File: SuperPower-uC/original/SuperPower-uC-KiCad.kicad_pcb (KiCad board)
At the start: 2 copper layers, 95 x 42 mm, 172 parts, among them J1 JST_PH_S2B_thru, J11 Conn_01x02_Male, J12 Conn_01x02_Male, J13 Conn_01x02_Male, J2 Barrel_Jack_Switch, J3 Conn_01x02_Male, J4 DNP/JST_ZH_S2B_thru, J5 JST_XH_S2B_thru, J6 Conn_01x02_Male, J7 Conn_01x19_Female, J8 Conn_01x19_Female, Q1 DMN2019UTS, Q10 2N7002A, Q11 2N7002A, Q12 DMP2035UVT, Q13 DMP2035UVT, Q14 DMP2035UVT, Q2 DMP3028LSD, Q3 DMN3018SSD, Q4 2N7002A, Q5 DMP2035UVT, Q6 BSS84-7-F, Q7 S8050, Q8 S8050, Q9 2N7002A, SW1 DNP/SKRKAEE020, U1 AP9101CK6-AYTRG1, U10 TPS63070RNMT, U2 USB-C, U3 IP4220CZ6, U4 LTC4162EUFD-LAD, U5 RV-3028-C7, U6 CP2102N-A01-GQFN28, U7 ESP32-WROOM32, U8 TPS70933DRVT, U9 TPS63070RNMT

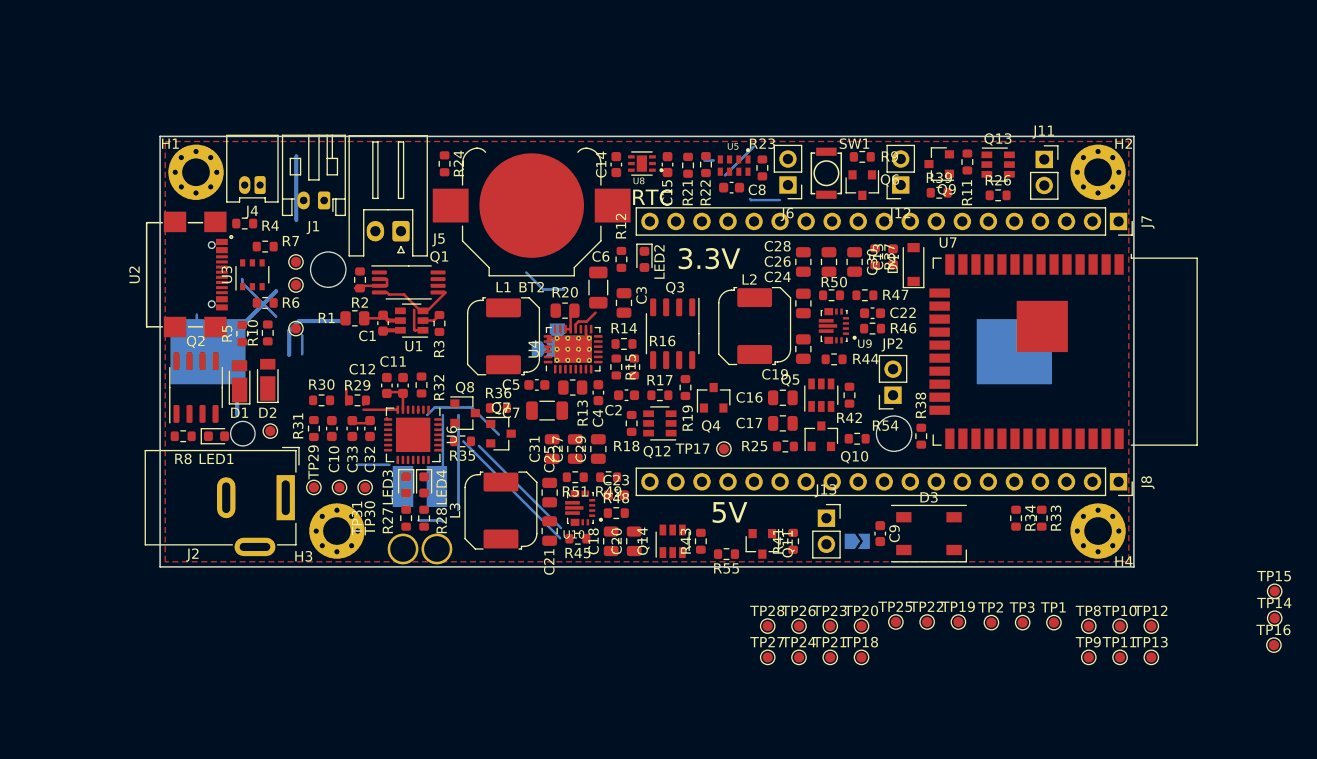
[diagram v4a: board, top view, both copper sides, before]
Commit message: Add some DIP switch 1 way (x3)
+ add optionnal on board 0603 NTC + misc.
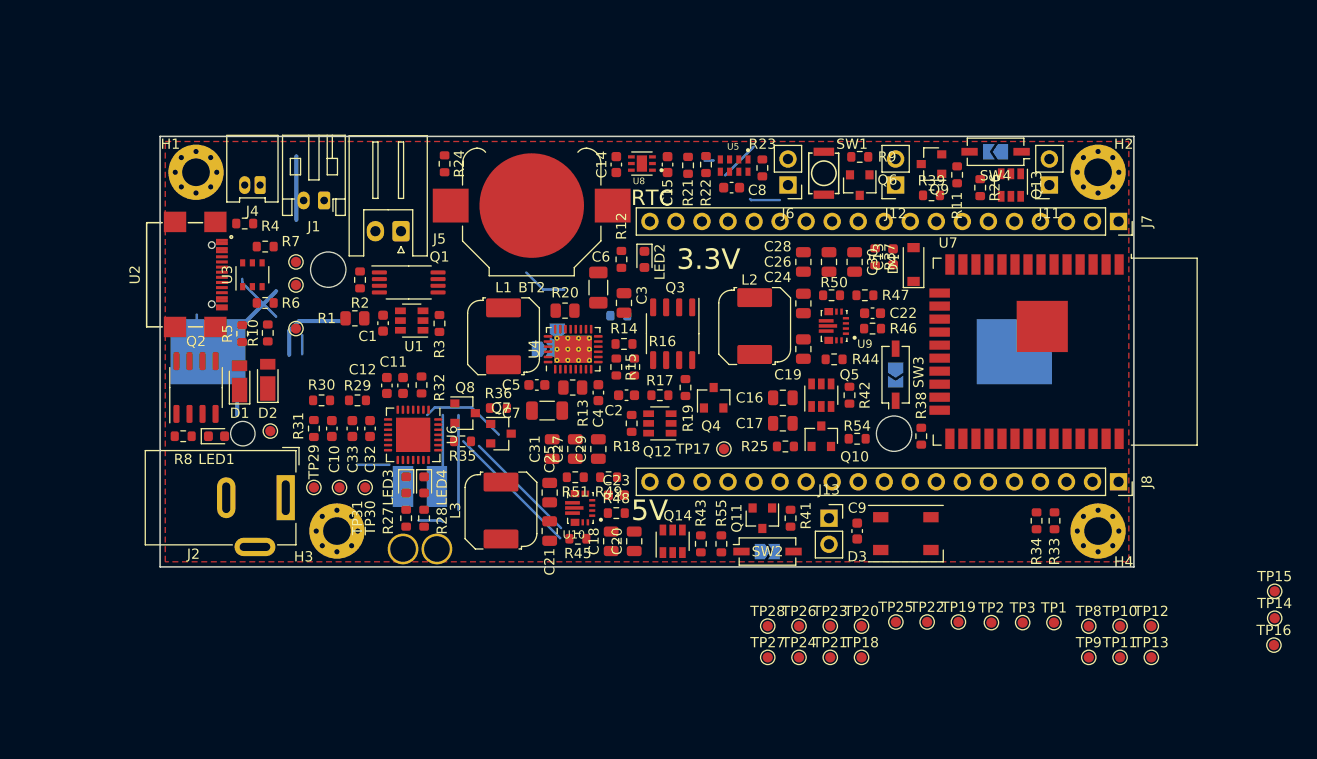
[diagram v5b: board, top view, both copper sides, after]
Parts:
- added JP4: SolderJumper_2_Open, Jumper:SolderJumper-2_P1.3mm_Open_TrianglePad1.0x1.5mm, B.Cu at (191.5, 35.5)
- added SW2: SW_DIP_x01, Button_Switch_SMD:SW_DIP_SPSTx01_Slide_Copal_CHS-01A_W5.08mm_P1.27mm_JPin, F.Cu at (169.2, 74.5)
- added SW3: SW_DIP_x01, Button_Switch_SMD:SW_DIP_SPSTx01_Slide_Copal_CHS-01A_W5.08mm_P1.27mm_JPin, F.Cu at (181.8, 57.2)
- added SW4: SW_DIP_x01, Button_Switch_SMD:SW_DIP_SPSTx01_Slide_Copal_CHS-01A_W5.08mm_P1.27mm_JPin, F.Cu at (191.5, 35.5)
- added TH1: DNP/NB21J50103JBB, Resistor_SMD:R_0603_1608Metric, B.Cu at (154.8, 51.5)
- JP2: value Jumper_NC_Small -> SolderJumper_2_Open; footprint Connector_PinSocket_2.54mm:PinSocket_1x02_P2.54mm_Vertical -> Jumper:SolderJumper-2_P1.3mm_Open_TrianglePad1.0x1.5mm; moved to B.Cu
- JP3: value Jumper_NC_Small -> SolderJumper_2_Open
- moved JP3 8.83 mm to (169.2, 74.5)
- moved J11 2.55 mm to (196.8, 38.8), turned to 180 degrees
- moved Q11 2.50 mm to (168.8, 71.2)
- moved Q13 2.36 mm to (193.0, 38.8), turned to 270 degrees
- moved C9 2.26 mm to (178.0, 72.5)
- moved R41 2.26 mm to (171.5, 71.2)
- moved D3 2.25 mm to (182.8, 72.8)
- moved R34 2.02 mm to (195.5, 71.5)
- moved JP2 1.99 mm to (181.8, 57.3), turned to 270 degrees
- moved R26 1.90 mm to (190.0, 39.0), turned to 270 degrees
- moved R11 1.60 mm to (187.8, 37.8)
- moved R33 1.27 mm to (197.2, 71.5)
- moved R55 1.12 mm to (164.8, 73.8), turned to 270 degrees
- moved R39 0.79 mm to (185.2, 39.8)
- moved Q9 0.75 mm to (185.2, 36.7)
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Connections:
- net Net-(JP3-Pad1) renamed /Regulator and Cut-Off Module/5v_OnOff
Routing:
- net /Battery Module/CO: track 6.36 -> 0.00 mm
- net -BATT: track 5.62 -> 0.00 mm
- net Net-(C1-Pad1): track 3.87 -> 0.00 mm
- net /VBUS1: track 5.22 -> 1.85 mm
- net /MCU Module/Vbus: track 3.31 -> 0.00 mm
- net GND: track 8.44 -> 5.23 mm
- net /Charging Module/CELLS1: track 2.88 -> 0.00 mm
- net /Battery Module/DO: track 2.81 -> 0.00 mm
- net /MCU Module/VIO: track 2.72 -> 0.00 mm
- net +BATT: track 21.8 -> 19.5 mm
- net /Battery Module/VM: track 1.83 -> 0.00 mm
- net /Charging Module/SW: track 0.50 -> 0.00 mm

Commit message: Misc.
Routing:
- net /MCU Module/TXD: track 29.0 -> 0.00 mm
- net +BATT: track 19.5 -> 0.00 mm
- net /Charger inputs and USB IO/V_CHARGE: track 13.9 -> 0.00 mm
- net /MCU Module/RXD: track 13.4 -> 0.00 mm
- net VDD: track 7.70 -> 0.00 mm
- net Net-(Q1-Pad5): track 6.22 -> 0.00 mm
- net GND: track 5.23 -> 0.00 mm
- net Net-(L1-Pad2): track 4.37 -> 0.00 mm
- net /RTC/~INT: track 3.95 -> 0.00 mm
- net /Charging Module/3v3_I2C: track 2.94 -> 0.00 mm
- net /MCU Module/RSTb: track 2.44 -> 0.00 mm
- net /VBUS1: track 1.85 -> 0.00 mm
- net /SCL: track 0.89 -> 0.00 mm
